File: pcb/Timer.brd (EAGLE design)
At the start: 68.6 x 68.6 mm, 42 parts, among them Q1 8MHz, U1 ATTINY24SSU, U2 SCT2024CSOG, U3 SCT2024CSOG, U4 LD117AS33TR

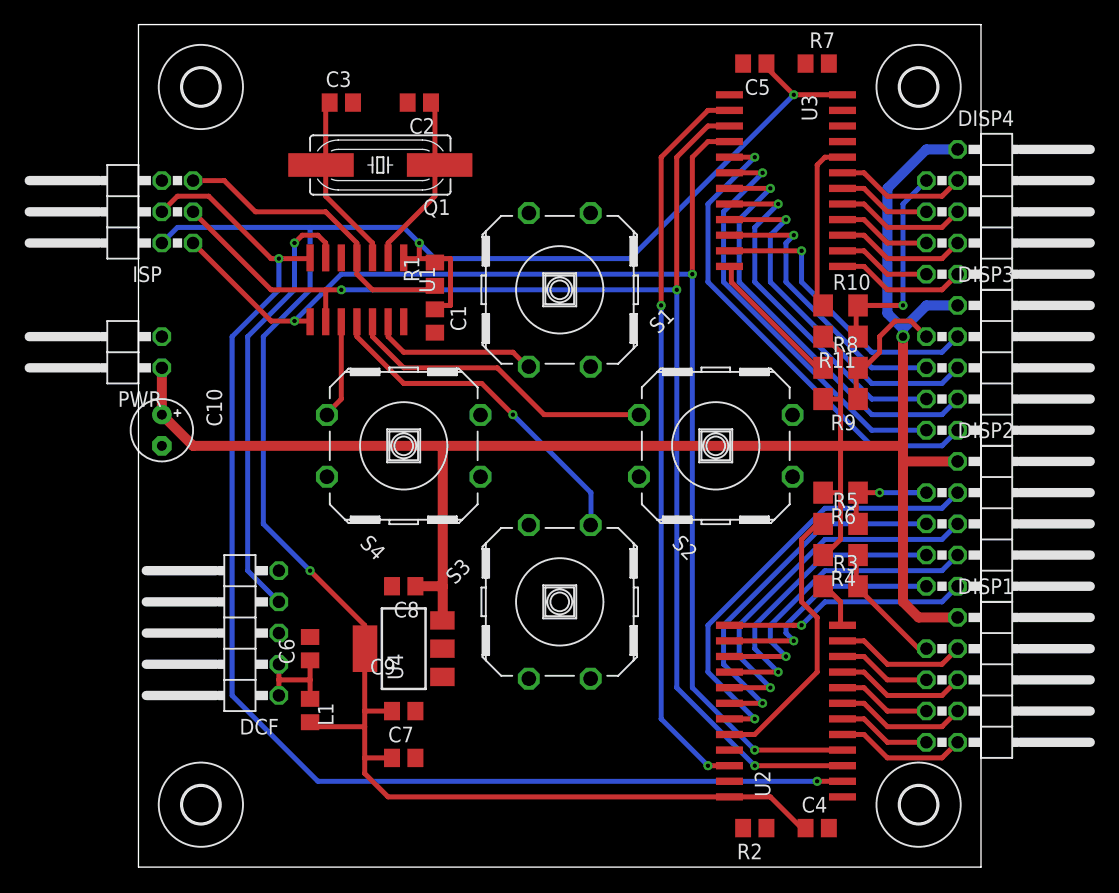
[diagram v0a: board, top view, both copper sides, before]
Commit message: Add Extension connector, move some traces
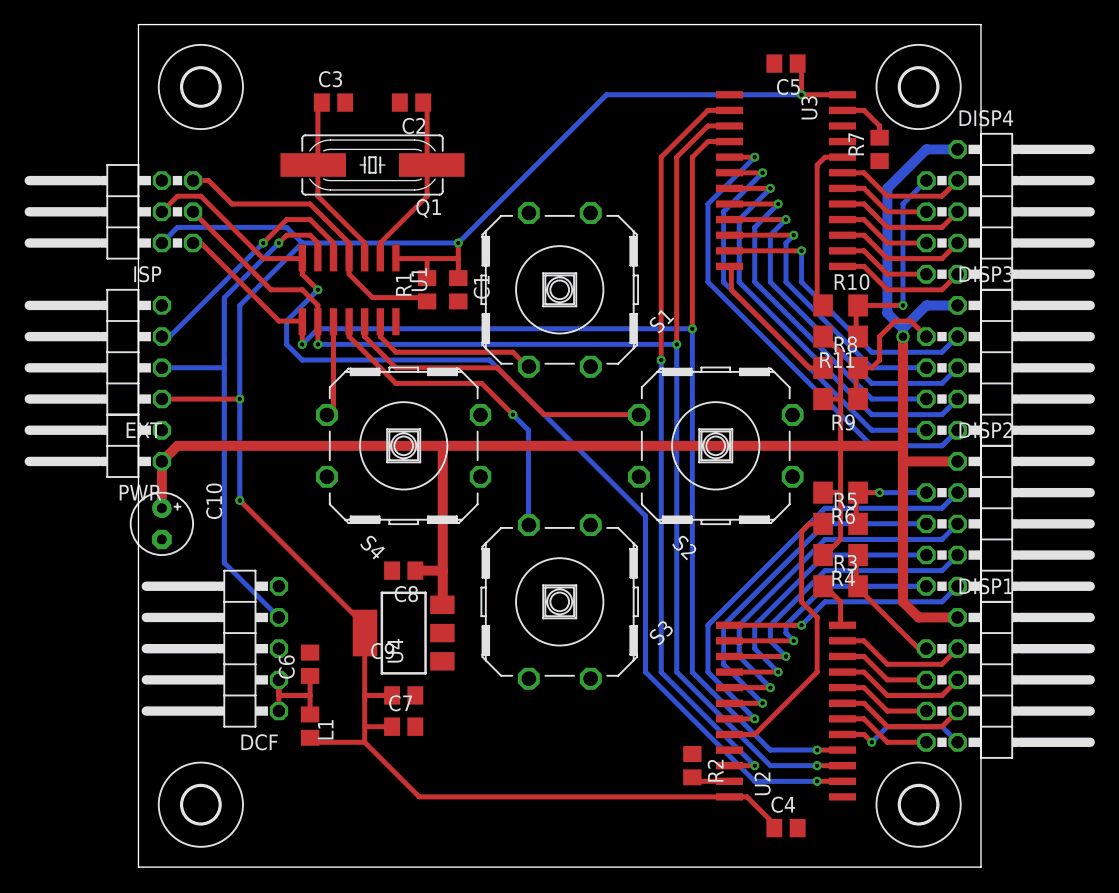
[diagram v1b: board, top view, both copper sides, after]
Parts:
- added EXT: (no value), pinhead-2:1X04/90
- moved R7 8.64 mm to (60.3, 58.4), turned to 90 degrees
- moved C10 7.62 mm to (1.91, 27.9)
- moved PWR 7.62 mm to (-1.91, 34.3)
- moved R2 7.18 mm to (45.1, 8.26), turned to 270 degrees
- moved C1 3.18 mm to (26.0, 47.0)
- moved C4 2.54 mm to (52.7, 3.17)
- moved C5 2.54 mm to (52.7, 65.4)
- moved C7 2.54 mm to (21.6, 11.4)
- moved R1 1.42 mm to (23.5, 47.0)
- moved C9 1.27 mm to (21.6, 14.0)
- moved C6 1.27 mm to (14.0, 16.5)
- moved C8 1.27 mm to (21.6, 24.1)
- moved DCF 1.27 mm to (7.62, 17.8)
- moved L1 1.27 mm to (14.0, 11.5)
- moved U4 1.27 mm to (21.6, 19.1)
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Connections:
- new net EXT: EXT.3, U1.5
- net DCF: now also EXT.2
- net GND: now also EXT.4
- net SW-D: no longer S3.4
- net SW-L: no longer S4.3
- net SW-R: no longer S2.3
- net SW-U: no longer S1.3
- net VCC: now also EXT.1
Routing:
- net EXT: track 0.00 -> 19.9 mm, vias 0 -> 1
- net MOSI/SDI: track 104.5 -> 90.1 mm
- net DCF: track 36.1 -> 44.2 mm
- net N$37: track 0.00 -> 4.50 mm
- net N$38: track 0.00 -> 3.15 mm
- net SDO/SDI: track 60.0 -> 61.9 mm
- net VDD: track 159.5 -> 157.7 mm
- net SW-D: track 28.1 -> 26.7 mm
- net N$3: track 8.21 -> 9.49 mm
- net MISO/LA: track 107.2 -> 106.0 mm
- net SW-U: track 13.8 -> 14.4 mm
- net SW-R: track 25.5 -> 26.2 mm
- net VCC: vias 3 -> 4
- net N$4: vias 0 -> 1

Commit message: Add ground planes
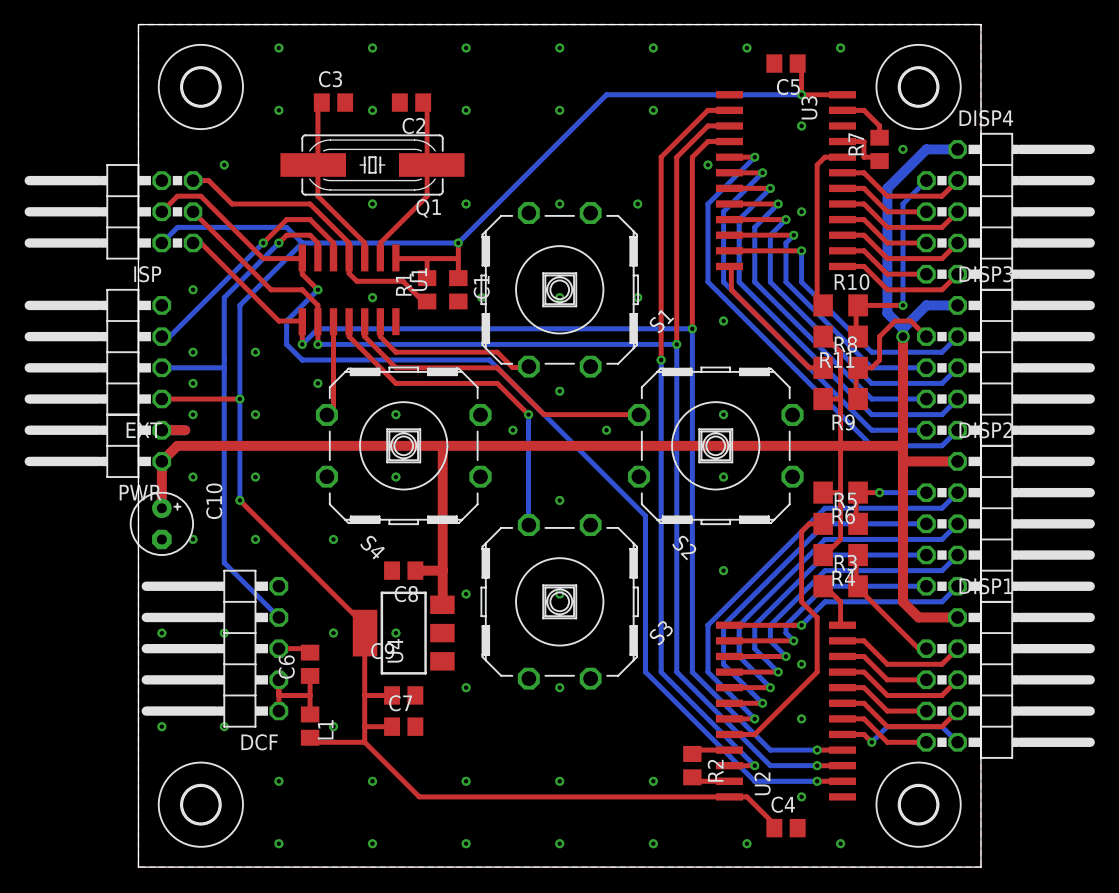
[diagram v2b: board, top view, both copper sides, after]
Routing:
- net GND: track 0.00 -> 14.1 mm, vias 0 -> 73
- net SW-D: track 26.7 -> 27.4 mm
- added copper zone on layer 1, net GND
- added copper zone on layer 16, net GND

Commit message: Update footprints and silkscreen
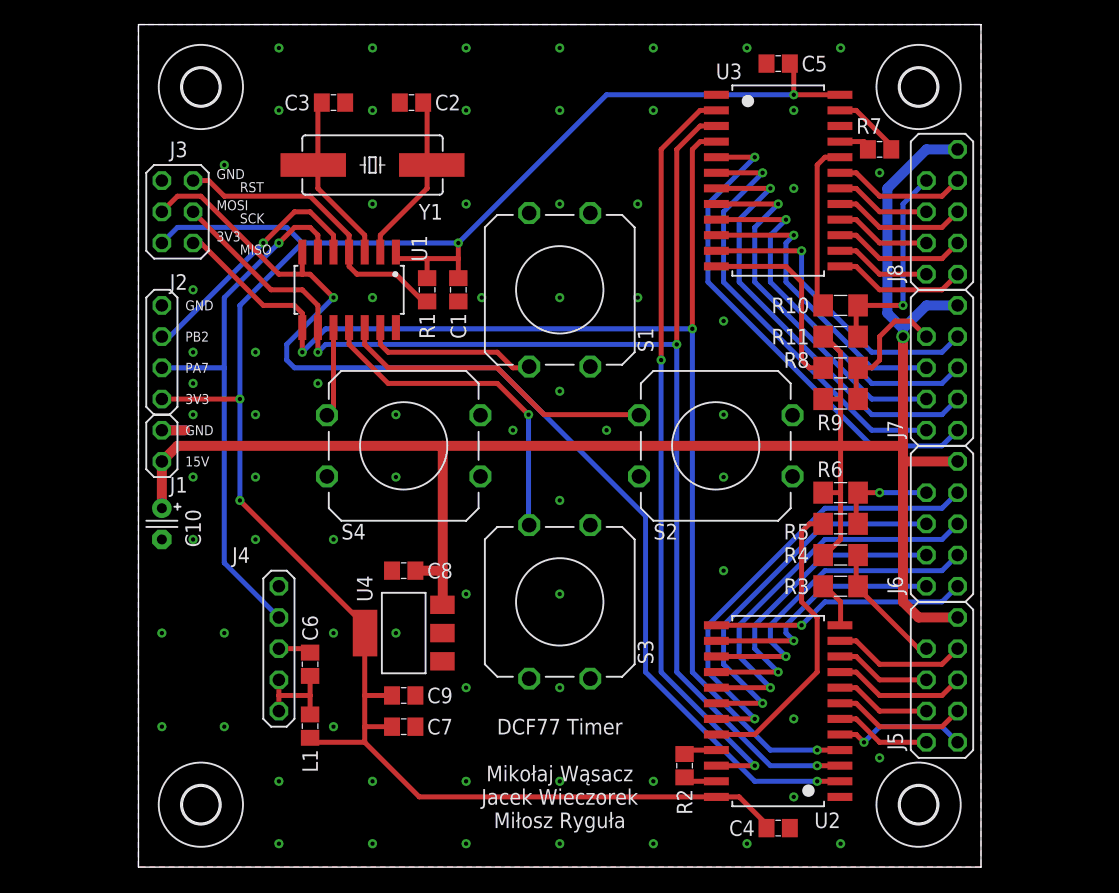
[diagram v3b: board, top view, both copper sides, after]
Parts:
- removed DCF: (no value), pinhead-2:1X05/90
- removed DISP1, DISP2, DISP3, DISP4: (no value), .MW:DISP-CON
- removed EXT: (no value), pinhead-2:1X04/90
- removed ISP: (no value), pinhead-2:2X03/90
- removed PWR: (no value), pinhead-2:1X02/90
- removed Q1: 8MHz, crystal:HC49UP
- added J1: PWR, .pinhead:1X02/90
- added J2: EXT, .pinhead:1X04/90
- added J3: ISP, .pinhead:2X03/90
- added J4: DCF77, .pinhead:1X05/90
- added J5: DISP1, .pinhead:2X04/05/90
- added J6: DISP2, .pinhead:2X04/05/90
- added J7: DISP3, .pinhead:2X04/05/90
- added J8: DISP4, .pinhead:2X04/05/90
- added Y1: 8MHz, .crystal:HC49UP
- C1, C2, C3, C4, C5, C6, C7, C8, C9: device rcl:C0805 -> .rcl:C0805
- C10: device rcl:E2,5-5 -> .rcl:E2,5
- H1, H2, H3, H4: value MOUNT-HOLE3.0 -> 3.0
- L1: device .MW:L0805 -> .rcl:L0805
- R1, R2, R7: device rcl:R0805 -> .rcl:R0805
- R10, R11, R3, R4, R5, R6, R8, R9: device rcl:R1206 -> .rcl:R1206
- S1: value RACON12/ -> U; device switch-misc:RACON12/ -> .switch:TACT-12
- S2: value RACON12/ -> R; device switch-misc:RACON12/ -> .switch:TACT-12
- S3: value RACON12/ -> D; device switch-misc:RACON12/ -> .switch:TACT-12
- S4: value RACON12/ -> L; device switch-misc:RACON12/ -> .switch:TACT-12
- U1: device .MW:SO14 -> .atmel:SO14
- U2, U3: device .MW:SO24W -> .starchips:SO24W
- U4: device v-reg:SOT223 -> .v-reg:SOT223
- moved C4 0.63 mm to (52.1, 3.17)
- moved C5 0.63 mm to (52.1, 65.4)
- moved R2 0.63 mm to (44.5, 8.26)
- moved U2 0.63 mm to (52.1, 12.7)
- moved U3 0.63 mm to (52.1, 55.9)
- turned R7 to 0 degrees
- turned S1 to 270 degrees
- turned S2 to 180 degrees
- turned S3 to 270 degrees
- turned S4 to 180 degrees
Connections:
- net DCF: now also J2.2, J4.4; no longer DCF.4, EXT.2
- net EXT: now also J2.3; no longer EXT.3
- net GND: now also J1.2, J2.4, J3.6, J4.3, J4.5; no longer DCF.3, DCF.5, EXT.4, ISP.6, PWR.2
- net MISO/LA: now also J3.1; no longer ISP.1
- net MOSI/SDI: now also J3.4; no longer ISP.4
- net N$1: now also Y1.2; no longer Q1.2
- net N$10: now also J5.8; no longer DISP1.8
- net N$11: now also J5.7; no longer DISP1.7
- net N$13: now also J6.2; no longer DISP2.2
- net N$14: now also J7.1; no longer DISP3.1
- net N$15: now also J7.3; no longer DISP3.3
- net N$16: now also J7.5; no longer DISP3.5
- net N$17: now also J7.7; no longer DISP3.7
- net N$18: now also J7.2; no longer DISP3.2
- net N$19: now also J7.4; no longer DISP3.4
- net N$2: now also Y1.1; no longer Q1.1
- net N$20: now also J7.6; no longer DISP3.6
- net N$21: now also J7.8; no longer DISP3.8
- net N$22: now also J6.4; no longer DISP2.4
- net N$24: now also J8.2; no longer DISP4.2
- net N$25: now also J8.4; no longer DISP4.4
- net N$26: now also J8.6; no longer DISP4.6
- net N$28: now also J8.8; no longer DISP4.8
- net N$3: now also J4.1, J4.2; no longer DCF.1, DCF.2
- net N$30: now also J8.1; no longer DISP4.1
- net N$31: now also J8.3; no longer DISP4.3
- net N$32: now also J8.5; no longer DISP4.5
- net N$33: now also J6.6; no longer DISP2.6
- net N$34: now also J6.8; no longer DISP2.8
- net N$35: now also J6.7; no longer DISP2.7
- net N$36: now also J6.5; no longer DISP2.5
- net N$39: now also J6.3; no longer DISP2.3
- net N$4: now also J5.1; no longer DISP1.1
- net N$40: now also J6.1; no longer DISP2.1
- net N$42: now also J8.7; no longer DISP4.7
- net N$5: now also J5.2; no longer DISP1.2
- net N$6: now also J5.3; no longer DISP1.3
- net N$7: now also J5.4; no longer DISP1.4
- net N$8: now also J5.5; no longer DISP1.5
- net N$9: now also J5.6; no longer DISP1.6
- net RST: now also J3.5; no longer ISP.5
- net SCK/CLK: now also J3.3; no longer ISP.3
- net VCC: now also J2.1, J3.2; no longer EXT.1, ISP.2
- net VDD: now also J1.1, J5.9, J6.9, J7.9, J8.9; no longer DISP1.9, DISP2.9, DISP3.9, DISP4.9, PWR.1
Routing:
- net N$23: track 12.1 -> 15.8 mm
- net MOSI/SDI: track 90.1 -> 93.1 mm
- net N$34: track 10.1 -> 8.23 mm
- net GND: track 14.1 -> 12.4 mm, vias 73 -> 72
- net N$3: track 9.49 -> 8.22 mm
- net N$37: track 4.50 -> 5.68 mm
- net N$41: track 23.2 -> 24.3 mm
- net N$40: track 19.9 -> 20.9 mm
- net N$39: track 25.3 -> 26.3 mm
- net N$36: track 30.7 -> 31.7 mm
- net N$35: track 36.0 -> 37.1 mm
- net N$33: track 30.3 -> 31.4 mm
- net N$22: track 24.9 -> 26.0 mm
- net N$20: track 23.6 -> 24.7 mm
- net N$19: track 29.0 -> 30.1 mm
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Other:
- board text added: "15V"
- board text added: "3V3"
- board text added: "DCF77 Timer Mikołaj Wąsacz Jacek Wieczorek Miłosz Ryguła"
- board text added: "GND"
- board text added: "MISO"
- board text added: "MOSI"
- board text added: "PA7"
- board text added: "PB2"
- board text added: "RST"
- board text added: "SCK"

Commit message: Fix errors, move components to a common library
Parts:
- added R12: 1, Timer:R0805
- C1, C2, C3, C4, C5, C6, C7, C8, C9: device .rcl:C0805 -> Timer:C0805
- C10: device .rcl:E2,5 -> Timer:E2,5
- J1: device .pinhead:1X02/90 -> Timer:1X02/90
- J2: device .pinhead:1X04/90 -> Timer:1X04/90
- J3: device .pinhead:2X03/90 -> Timer:2X03/90
- J4: device .pinhead:1X05/90 -> Timer:1X05/90
- J5, J6, J7, J8: device .pinhead:2X04/05/90 -> Timer:2X04/05/90
- L1: device .rcl:L0805 -> Timer:L0805
- R1, R2, R7: device .rcl:R0805 -> Timer:R0805
- R10, R5: value 430 -> 680; device .rcl:R1206 -> Timer:R1206
- R11, R6: value 750 -> 680; device .rcl:R1206 -> Timer:R1206
- R3, R8: value 430 -> 360; device .rcl:R1206 -> Timer:R1206
- R4, R9: value 750 -> 360; device .rcl:R1206 -> Timer:R1206
- S1, S2, S3, S4: device .switch:TACT-12 -> Timer:TACT-12
- U1: device .atmel:SO14 -> Timer:SO14
- U2, U3: device .starchips:SO24W -> Timer:SO24W
- U4: value LD117AS33TR -> LM1117-3.3; device .v-reg:SOT223 -> Timer:SOT223
- Y1: device .crystal:HC49UP -> Timer:HC49UP
- moved R10 7.62 mm to (57.1, 38.1)
- moved R9 7.62 mm to (57.1, 45.7)
- moved L1 2.54 mm to (16.5, 11.4), turned to 90 degrees
- moved R11 2.54 mm to (57.1, 40.6), turned to 0 degrees
- moved R8 2.54 mm to (57.1, 43.2), turned to 180 degrees
- moved H3 1.80 mm to (3.81, 3.81)
- moved H2 1.80 mm to (64.8, 3.81)
- moved H4 1.80 mm to (3.81, 64.8)
- moved H1 1.80 mm to (64.8, 64.8)
- moved R7 1.42 mm to (59.7, 59.7), turned to 90 degrees
- turned R3 to 180 degrees
- turned R6 to 0 degrees
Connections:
- removed net MISO/LA: J3.1, U1.8, U2.4, U3.4
- removed net MOSI/SDI: J3.4, U1.7, U2.2
- new net MISO/SDI: J3.1, U1.8, U2.2
- new net MOSI/LA: J3.4, U1.7, U2.4, U3.4
- new net N$29: L1.1, R12.1
- net N$10: now also R3.1; no longer R3.2, R4.1
- net N$12: now also R3.2, R5.1; no longer R3.1
- net N$21: now also R8.1; no longer R8.2, R9.1
- net N$23: now also R10.1, R8.2; no longer R8.1
- net N$27: now also R11.1, R9.2; no longer R10.1
- net N$28: now also R9.1; no longer R10.2, R11.1
- net N$3: now also R12.2; no longer L1.1
- net N$34: now also R4.1; no longer R5.2, R6.1
- net N$41: now also R4.2, R6.1; no longer R5.1
- net VCC: now also U4.2
- net VDD: now also R10.2, R5.2; no longer R4.2, R9.2
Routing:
- net MOSI/LA: track 0.00 -> 109.4 mm, vias 0 -> 3
- net MISO/LA: track 106.4 -> 0.00 mm, vias 3 -> 0
- net MOSI/SDI: track 93.1 -> 0.00 mm, vias 2 -> 0
- net MISO/SDI: track 0.00 -> 80.1 mm, vias 0 -> 2
- net VDD: track 157.7 -> 149.0 mm
- net N$27: track 13.7 -> 20.2 mm
- net N$12: track 3.90 -> 10.4 mm
- net N$21: track 11.4 -> 6.62 mm
- net N$41: track 24.3 -> 28.6 mm
- net N$23: track 15.8 -> 20.1 mm
- net VCC: track 172.1 -> 175.9 mm
- net N$29: track 0.00 -> 2.79 mm
- net N$37: track 5.68 -> 2.99 mm
- net N$10: track 10.4 -> 7.76 mm
- net N$28: track 17.3 -> 14.6 mm
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
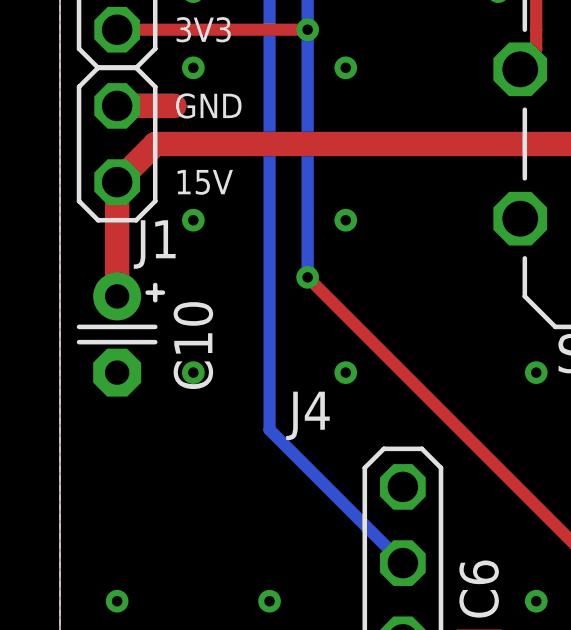
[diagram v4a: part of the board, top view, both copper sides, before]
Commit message: Change C6 value
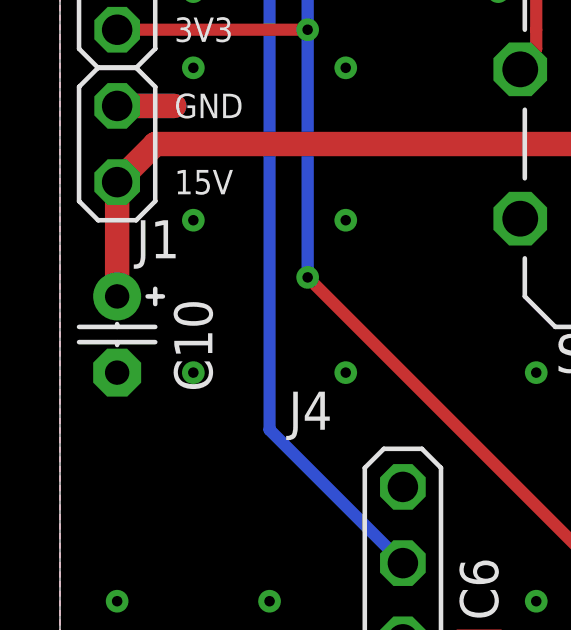
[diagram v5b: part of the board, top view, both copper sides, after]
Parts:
- C6: value 100nF -> 10uF
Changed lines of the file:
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@@
 <layer number="45" name="Holes" color="7" fill="1" visible="yes" active="yes"/>
 <layer number="46" name="Milling" color="3" fill="1" visible="no" active="yes"/>
-<layer number="47" name="Measures" color="7" fill="1" visible="yes" active="yes"/>
+<layer number="47" name="Measures" color="7" fill="1" visible="no" active="yes"/>
 <layer number="48" name="Document" color="7" fill="1" visible="no" active="yes"/>
 <layer number="49" name="Reference" color="7" fill="1" visible="no" active="yes"/>
@@
 <attribute name="NAME" x="53.975" y="64.77" size="1.27" layer="25"/>
 </element>
-<element name="C6" library="Timer" package="C0805" value="100nF" x="13.97" y="16.51" smashed="yes" rot="R90">
+<element name="C6" library="Timer" package="C0805" value="10uF" x="13.97" y="16.51" smashed="yes" rot="R90">
 <attribute name="NAME" x="14.605" y="18.415" size="1.27" layer="25" rot="R90"/>
 </element>
